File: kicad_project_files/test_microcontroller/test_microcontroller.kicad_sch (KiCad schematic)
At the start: 44 parts, among them J1 USB_C_Receptacle_USB2.0, SW1 SW_Push, SW2 SW_Push, SW3 SW_Push, SW4 SW_Push, SW5 SW_Push, SW6 SW_Push, SW7 SW_Push, SW8 SW_Push, SW9 SW_Push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

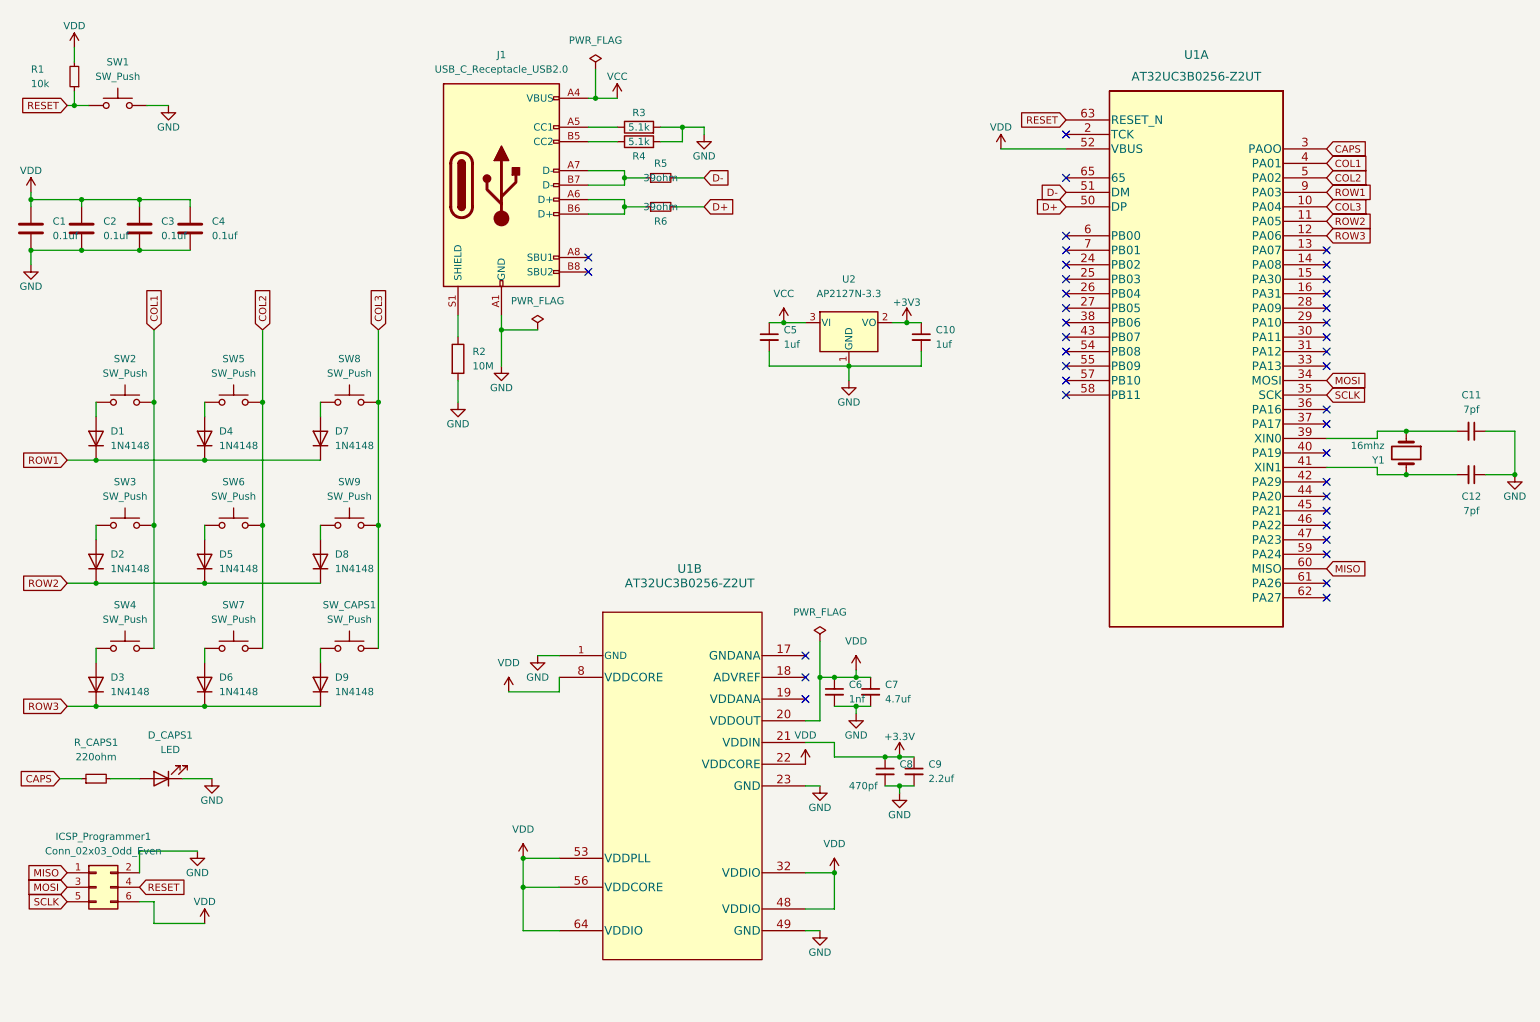
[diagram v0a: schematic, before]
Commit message: update to utmega8u2
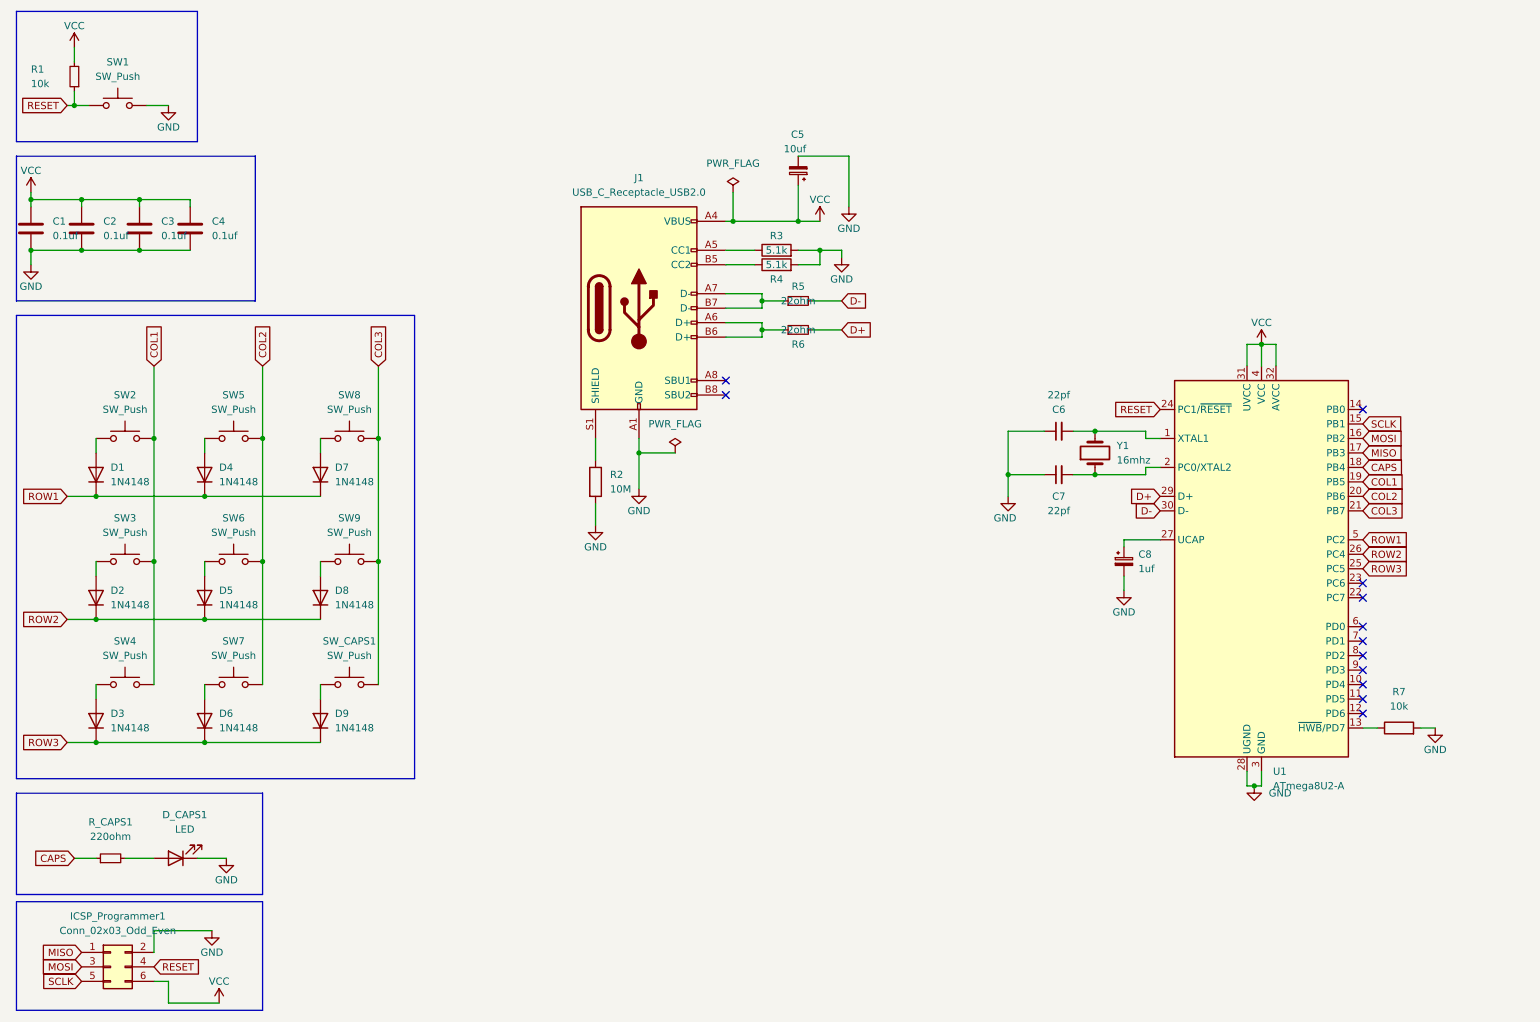
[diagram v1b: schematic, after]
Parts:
- removed C10, C5: 1uf, Capacitor_THT:CP_Radial_D4.0mm_P1.50mm, symbol Device:C_Small
- removed C11, C12: 7pf, Capacitor_THT:C_Disc_D3.0mm_W1.6mm_P2.50mm, symbol Device:C_Small
- removed C8: 470pf, symbol Device:C_Small
- removed C9: 2.2uf, symbol Device:C_Small
- removed U1: AT32UC3B0256-Z2UT, QFN64-4_ATM, symbol AT32UC3B0256-Z2UT:AT32UC3B0256-Z2UT
- removed U2: AP2127N-3.3, Package_TO_SOT_SMD:SOT-23, symbol Regulator_Linear:AP2127N-3.3
- added C5: 10uf, Capacitor_THT:CP_Radial_D4.0mm_P1.50mm, symbol Device:C_Polarized_Small
- added C8: 1uf, Capacitor_THT:CP_Radial_D4.0mm_P1.50mm, symbol Device:C_Polarized_Small
- added R7: 10k, Resistor_THT:R_Axial_DIN0204_L3.6mm_D1.6mm_P5.08mm_Horizontal, symbol Device:R
- added U1: ATmega8U2-A, Package_QFP:TQFP-32_7x7mm_P0.8mm, symbol MCU_Microchip_ATmega:ATmega8U2-A
- C1, C2, C3, C4: footprint Capacitor_THT:C_Disc_D3.0mm_W1.6mm_P2.50mm -> Capacitor_THT:C_Rect_L7.0mm_W2.0mm_P5.00mm
- C6: value 1nf -> 22pf; footprint (none) -> Capacitor_THT:C_Disc_D3.0mm_W1.6mm_P2.50mm
- C7: value 4.7uf -> 22pf; footprint (none) -> Capacitor_THT:C_Disc_D3.0mm_W1.6mm_P2.50mm
- R5, R6: value 39ohm -> 22ohm
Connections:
- net CAPS: now also U1.18 (PB4)
- net COL1: now also U1.19 (PB5)
- net COL2: now also U1.20 (PB6)
- net COL3: now also U1.21 (PB7)
- net D+: now also U1.29 (D+)
- net D-: now also U1.30 (D-)
- net GND: now also C6.1, C7.1, C5.2, C8.2, R7.2, U1.28 (UGND), U1.3 (GND); no longer C6.2, C7.2
- net MISO: now also U1.17 (PB3)
- net MOSI: now also U1.16 (PB2)
- net RESET: now also U1.24 (PC1/~{RESET})
- net ROW1: now also U1.5 (PC2)
- net ROW2: now also U1.26 (PC4)
- net ROW3: now also U1.25 (PC5)
- net SCLK: now also U1.15 (PB1)
- net VCC: now also C1.1, C2.1, C3.1, C4.1, ICSP_Programmer1.6 (Pin_6), R1.2, C5.1, U1.31 (UVCC), U1.32 (AVCC), U1.4 (VCC)
- net at Y1.1: now also C7.2, U1.2 (PC0/XTAL2)
- net at Y1.2: now also C6.2, U1.1 (XTAL1)
- removed net VDD: C1.1, C2.1, C3.1, C4.1, C6.1, C7.1, ICSP_Programmer1.6 (Pin_6), R1.2
- new net: C8.1, U1.27 (UCAP)
- new net: R7.1, U1.13 (~{HWB}/PD7)
- no-connect marks 39 -> 12
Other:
- moved on the sheet: D1, D2, D3, D4, D5, D6, D7, D8, D9, D_CAPS1, ICSP_Programmer1, J1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

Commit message: update schematic
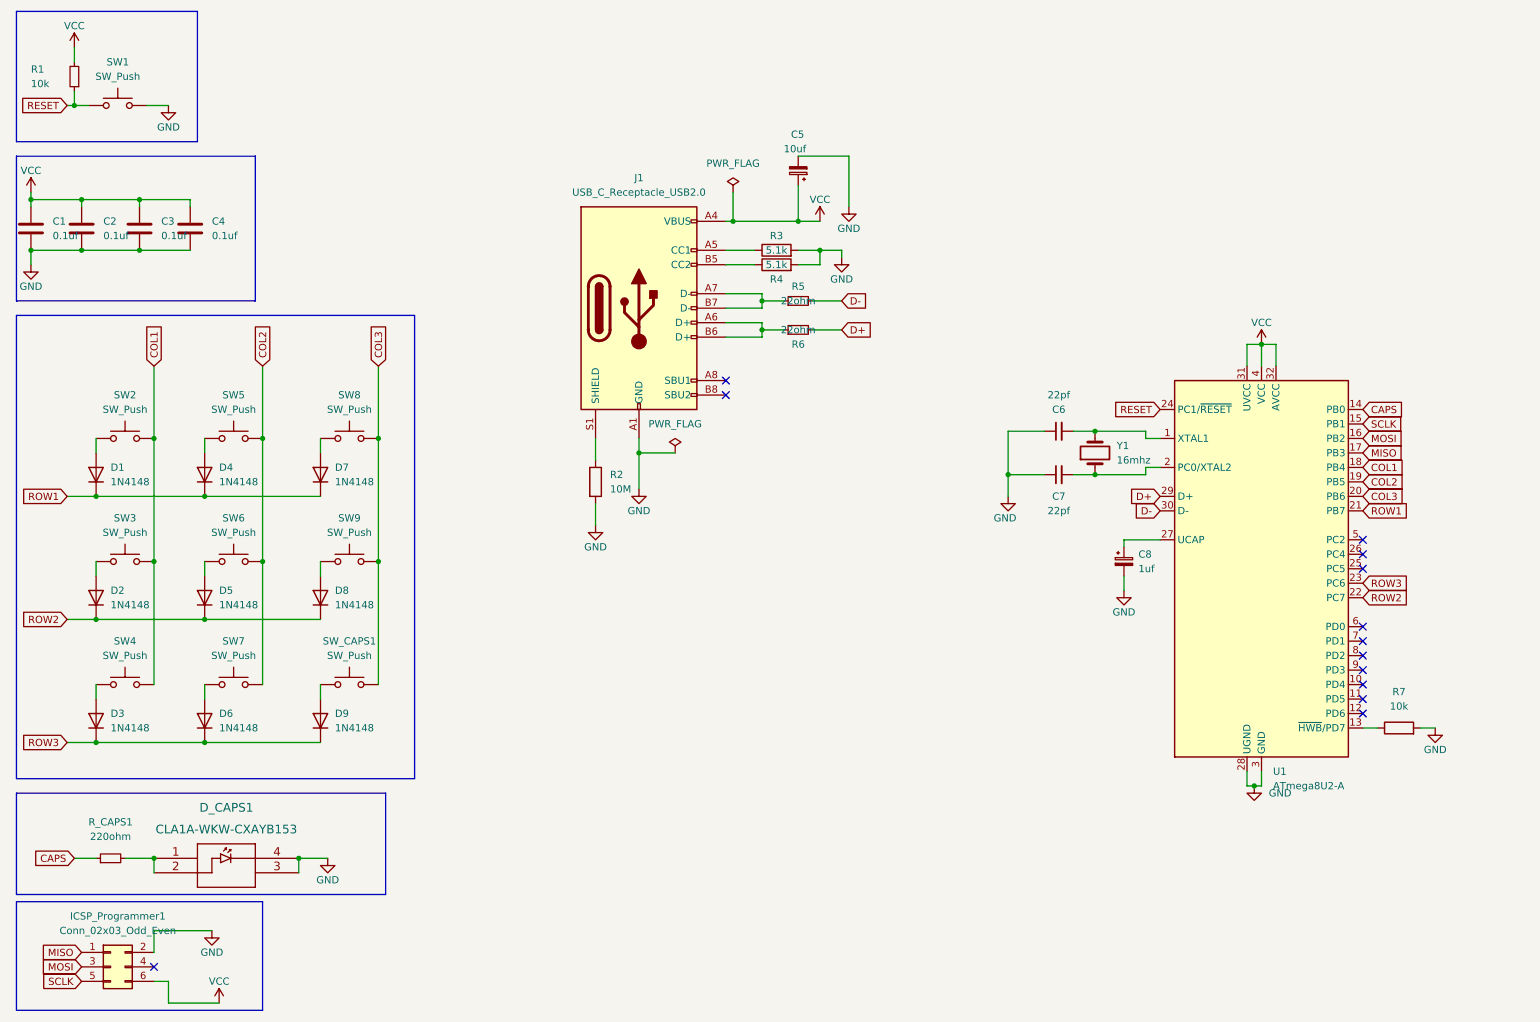
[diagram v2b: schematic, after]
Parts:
- removed D_CAPS1: LED, LED_THT:LED_D3.0mm, symbol Device:LED
- added D_CAPS1: CLA1A-WKW-CXAYB153, LED_SMD:LED_Cree-PLCC4_3.2x2.8mm_CCW, symbol CLA1A-WKW-CXAYB153 (SMD_LED):CLA1A-WKW-CXAYB153
- Y1: footprint Crystal:Crystal_HC49-4H_Vertical -> Crystal:Crystal_SMD_HC49-SD
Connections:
- net CAPS: now also U1.14 (PB0); no longer U1.18 (PB4)
- net COL1: now also U1.18 (PB4); no longer U1.19 (PB5)
- net COL2: now also U1.19 (PB5); no longer U1.20 (PB6)
- net COL3: now also U1.20 (PB6); no longer U1.21 (PB7)
- net GND: now also D_CAPS1.3, D_CAPS1.4
- net RESET: no longer ICSP_Programmer1.4 (Pin_4)
- net ROW1: now also U1.21 (PB7); no longer U1.5 (PC2)
- net ROW2: now also U1.22 (PC7); no longer U1.26 (PC4)
- net ROW3: now also U1.23 (PC6); no longer U1.25 (PC5)
- net at R_CAPS1.2: now also D_CAPS1.1, D_CAPS1.2
- no-connect marks 12 -> 13

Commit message: prof_pcb
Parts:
- SW2, SW3, SW4, SW5, SW6, SW7, SW8, SW9, SW_CAPS1: footprint Button_Switch_THT:SW_PUSH_6mm -> Button - Alternate:SW_4-1437565-0
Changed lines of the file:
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@@
     (property "Reference" "SW8" (id 0) (at 72.39 80.01 0))
     (property "Value" "SW_Push" (id 1) (at 72.39 82.55 0))
-    (property "Footprint" "Button_Switch_THT:SW_PUSH_6mm" (id 2) (at 72.39 82.55 0)
+    (property "Footprint" "Button - Alternate:SW_4-1437565-0" (id 2) (at 72.39 82.55 0)
       (effects (font (size 1.27 1.27)) hide)
     )
@@
     (property "Reference" "SW_CAPS1" (id 0) (at 72.39 123.19 0))
     (property "Value" "SW_Push" (id 1) (at 72.39 125.73 0))
-    (property "Footprint" "Button_Switch_THT:SW_PUSH_6mm" (id 2) (at 72.39 125.73 0)
+    (property "Footprint" "Button - Alternate:SW_4-1437565-0" (id 2) (at 72.39 125.73 0)
       (effects (font (size 1.27 1.27)) hide)
     )
@@
     (property "Reference" "SW7" (id 0) (at 52.07 123.19 0))
     (property "Value" "SW_Push" (id 1) (at 52.07 125.73 0))
-    (property "Footprint" "Button_Switch_THT:SW_PUSH_6mm" (id 2) (at 52.07 125.73 0)
+    (property "Footprint" "Button - Alternate:SW_4-1437565-0" (id 2) (at 52.07 125.73 0)
       (effects (font (size 1.27 1.27)) hide)
     )
@@
     (property "Reference" "SW2" (id 0) (at 33.02 80.01 0))
     (property "Value" "SW_Push" (id 1) (at 33.02 82.55 0))
-    (property "Footprint" "Button_Switch_THT:SW_PUSH_6mm" (id 2) (at 33.02 82.55 0)
+    (property "Footprint" "Button - Alternate:SW_4-1437565-0" (id 2) (at 33.02 82.55 0)
       (effects (font (size 1.27 1.27)) hide)
     )
@@
     (property "Reference" "SW4" (id 0) (at 33.02 123.19 0))
     (property "Value" "SW_Push" (id 1) (at 33.02 125.73 0))
-    (property "Footprint" "Button_Switch_THT:SW_PUSH_6mm" (id 2) (at 33.02 125.73 0)
+    (property "Footprint" "Button - Alternate:SW_4-1437565-0" (id 2) (at 33.02 125.73 0)
       (effects (font (size 1.27 1.27)) hide)
     )
@@
     (property "Reference" "SW6" (id 0) (at 52.07 101.6 0))
     (property "Value" "SW_Push" (id 1) (at 52.07 104.14 0))
-    (property "Footprint" "Button_Switch_THT:SW_PUSH_6mm" (id 2) (at 52.07 104.14 0)
+    (property "Footprint" "Button - Alternate:SW_4-1437565-0" (id 2) (at 52.07 104.14 0)
       (effects (font (size 1.27 1.27)) hide)
     )
@@
     (property "Reference" "SW3" (id 0) (at 33.02 101.6 0))
     (property "Value" "SW_Push" (id 1) (at 33.02 104.14 0))
-    (property "Footprint" "Button_Switch_THT:SW_PUSH_6mm" (id 2) (at 33.02 104.14 0)
+    (property "Footprint" "Button - Alternate:SW_4-1437565-0" (id 2) (at 33.02 104.14 0)
       (effects (font (size 1.27 1.27)) hide)
     )
@@
     (property "Reference" "SW9" (id 0) (at 72.39 101.6 0))
     (property "Value" "SW_Push" (id 1) (at 72.39 104.14 0))
-    (property "Footprint" "Button_Switch_THT:SW_PUSH_6mm" (id 2) (at 72.39 104.14 0)
+    (property "Footprint" "Button - Alternate:SW_4-1437565-0" (id 2) (at 72.39 104.14 0)
       (effects (font (size 1.27 1.27)) hide)
     )
@@
     (property "Reference" "SW5" (id 0) (at 52.07 80.01 0))
     (property "Value" "SW_Push" (id 1) (at 52.07 82.55 0))
-    (property "Footprint" "Button_Switch_THT:SW_PUSH_6mm" (id 2) (at 52.07 82.55 0)
+    (property "Footprint" "Button - Alternate:SW_4-1437565-0" (id 2) (at 52.07 82.55 0)
       (effects (font (size 1.27 1.27)) hide)
     )
@@
     )
     (path "/50ca629d-9549-4245-916f-2c4cae7c3f0a"
-      (reference "SW2") (unit 1) (value "SW_Push") (footprint "Button_Switch_THT:SW_PUSH_6mm")
+      (reference "SW2") (unit 1) (value "SW_Push") (footprint "Button - Alternate:SW_4-1437565-0")
     )
     (path "/9d7818bd-ddf7-4bad-b3c0-3aef487c2b7e"
-      (reference "SW3") (unit 1) (value "SW_Push") (footprint "Button_Switch_THT:SW_PUSH_6mm")
+      (reference "SW3") (unit 1) (value "SW_Push") (footprint "Button - Alternate:SW_4-1437565-0")
     )
     (path "/52d68fde-e730-4933-938c-d2c86e1b0ff1"
-      (reference "SW4") (unit 1) (value "SW_Push") (footprint "Button_Switch_THT:SW_PUSH_6mm")
+      (reference "SW4") (unit 1) (value "SW_Push") (footprint "Button - Alternate:SW_4-1437565-0")
     )
     (path "/f6abcdb5-c97b-4658-bdd0-3f9075e03d37"
-      (reference "SW5") (unit 1) (value "SW_Push") (footprint "Button_Switch_THT:SW_PUSH_6mm")
+      (reference "SW5") (unit 1) (value "SW_Push") (footprint "Button - Alternate:SW_4-1437565-0")
     )
     (path "/94f93b90-d7fb-4cff-b857-216e3985a961"
-      (reference "SW6") (unit 1) (value "SW_Push") (footprint "Button_Switch_THT:SW_PUSH_6mm")
+      (reference "SW6") (unit 1) (value "SW_Push") (footprint "Button - Alternate:SW_4-1437565-0")
     )
     (path "/4a9040f1-6dd6-41a1-895e-666cce1f9166"
-      (reference "SW7") (unit 1) (value "SW_Push") (footprint "Button_Switch_THT:SW_PUSH_6mm")
+      (reference "SW7") (unit 1) (value "SW_Push") (footprint "Button - Alternate:SW_4-1437565-0")
     )
     (path "/03bfc24c-91fd-4454-a173-f7bf00a01ff6"
-      (reference "SW8") (unit 1) (value "SW_Push") (footprint "Button_Switch_THT:SW_PUSH_6mm")
+      (reference "SW8") (unit 1) (value "SW_Push") (footprint "Button - Alternate:SW_4-1437565-0")
     )
     (path "/c36d20a4-c7cf-4667-ac3a-a69a07598eb6"
-      (reference "SW9") (unit 1) (value "SW_Push") (footprint "Button_Switch_THT:SW_PUSH_6mm")
+      (reference "SW9") (unit 1) (value "SW_Push") (footprint "Button - Alternate:SW_4-1437565-0")
     )
     (path "/13c19b45-90cd-497a-b404-81cf9319aa9e"
-      (reference "SW_CAPS1") (unit 1) (value "SW_Push") (footprint "Button_Switch_THT:SW_PUSH_6mm")
+      (reference "SW_CAPS1") (unit 1) (value "SW_Push") (footprint "Button - Alternate:SW_4-1437565-0")
     )
     (path "/b1833f54-dfb3-49c0-a81e-48d66c89dff0"

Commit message: pcb v1
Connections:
- net MISO: now also U1.6 (PD0); no longer U1.17 (PB3)
- net MOSI: now also U1.7 (PD1); no longer U1.16 (PB2)
- net SCLK: now also U1.8 (PD2); no longer U1.15 (PB1)
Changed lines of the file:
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@@
   (no_connect (at 138.43 77.47))
   (no_connect (at 138.43 80.01))
+  (no_connect (at 250.19 90.17))
   (no_connect (at 250.19 107.95))
   (no_connect (at 38.1 180.34))
+  (no_connect (at 250.19 87.63))
   (no_connect (at 250.19 110.49))
-  (no_connect (at 250.19 125.73))
   (no_connect (at 250.19 130.81))
   (no_connect (at 250.19 128.27))
   (no_connect (at 250.19 133.35))
   (no_connect (at 250.19 135.89))
-  (no_connect (at 250.19 123.19))
   (no_connect (at 250.19 105.41))
-  (no_connect (at 250.19 120.65))
+  (no_connect (at 250.19 85.09))
   (wire (pts (xy 40.64 182.88) (xy 40.64 186.69))
     (stroke (width 0) (type default) (color 0 0 0 0))
@@
     )
   )
-  (global_label "SCLK" (shape input) (at 250.19 85.09 0) (fields_autoplaced)
-    (effects (font (size 1.27 1.27)) (justify left))
-    (property "Intersheet References" "${INTERSHEET_REFS}" (id 0) (at 257.3807 85.0106 0)
+  (global_label "MOSI" (shape input) (at 250.19 123.19 0) (fields_autoplaced)
+    (effects (font (size 1.27 1.27)) (justify left))
+    (property "Intersheet References" "${INTERSHEET_REFS}" (id 0) (at 257.1993 123.1106 0)
       (effects (font (size 1.27 1.27)) (justify left) hide)
     )
@@
     )
   )
+  (global_label "SCLK" (shape input) (at 250.19 125.73 0) (fields_autoplaced)
+    (effects (font (size 1.27 1.27)) (justify left))
+    (property "Intersheet References" "${INTERSHEET_REFS}" (id 0) (at 257.3807 125.6506 0)
+      (effects (font (size 1.27 1.27)) (justify left) hide)
+    )
+  )
   (global_label "ROW2" (shape input) (at 22.86 119.38 180) (fields_autoplaced)
     (effects (font (size 1.27 1.27)) (justify right))
@@
     )
   )
+  (global_label "MISO" (shape input) (at 250.19 120.65 0) (fields_autoplaced)
+    (effects (font (size 1.27 1.27)) (justify left))
+    (property "Intersheet References" "${INTERSHEET_REFS}" (id 0) (at 257.1993 120.5706 0)
+      (effects (font (size 1.27 1.27)) (justify left) hide)
+    )
+  )
   (global_label "ROW3" (shape input) (at 250.19 113.03 0) (fields_autoplaced)
     (effects (font (size 1.27 1.27)) (justify left))
@@
     )
   )
-  (global_label "MOSI" (shape input) (at 250.19 87.63 0) (fields_autoplaced)
-    (effects (font (size 1.27 1.27)) (justify left))
-    (property "Intersheet References" "${INTERSHEET_REFS}" (id 0) (at 257.1993 87.5506 0)
-      (effects (font (size 1.27 1.27)) (justify left) hide)
-    )
-  )
   (global_label "COL2" (shape input) (at 57.15 74.93 90) (fields_autoplaced)
     (effects (font (size 1.27 1.27)) (justify left))
@@
       (effects (font (size 1.27 1.27)) (justify left) hide)
     )
-  )
-  (global_label "MISO" (shape input) (at 250.19 90.17 0) (fields_autoplaced)
-    (effects (font (size 1.27 1.27)) (justify left))
-    (property "Intersheet References" "${INTERSHEET_REFS}" (id 0) (at 257.1993 90.0906 0)
-      (effects (font (size 1.27 1.27)) (justify left) hide)
-    )
